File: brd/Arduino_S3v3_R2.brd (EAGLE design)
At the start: 49.1 x 49.1 mm, 35 parts, among them J4 USB_B_PTH, U1 FT232RL, U2 ATMEGA328P_TQFP, U3 ADXL337, Y2 CSTNE16M0V51Z000R0

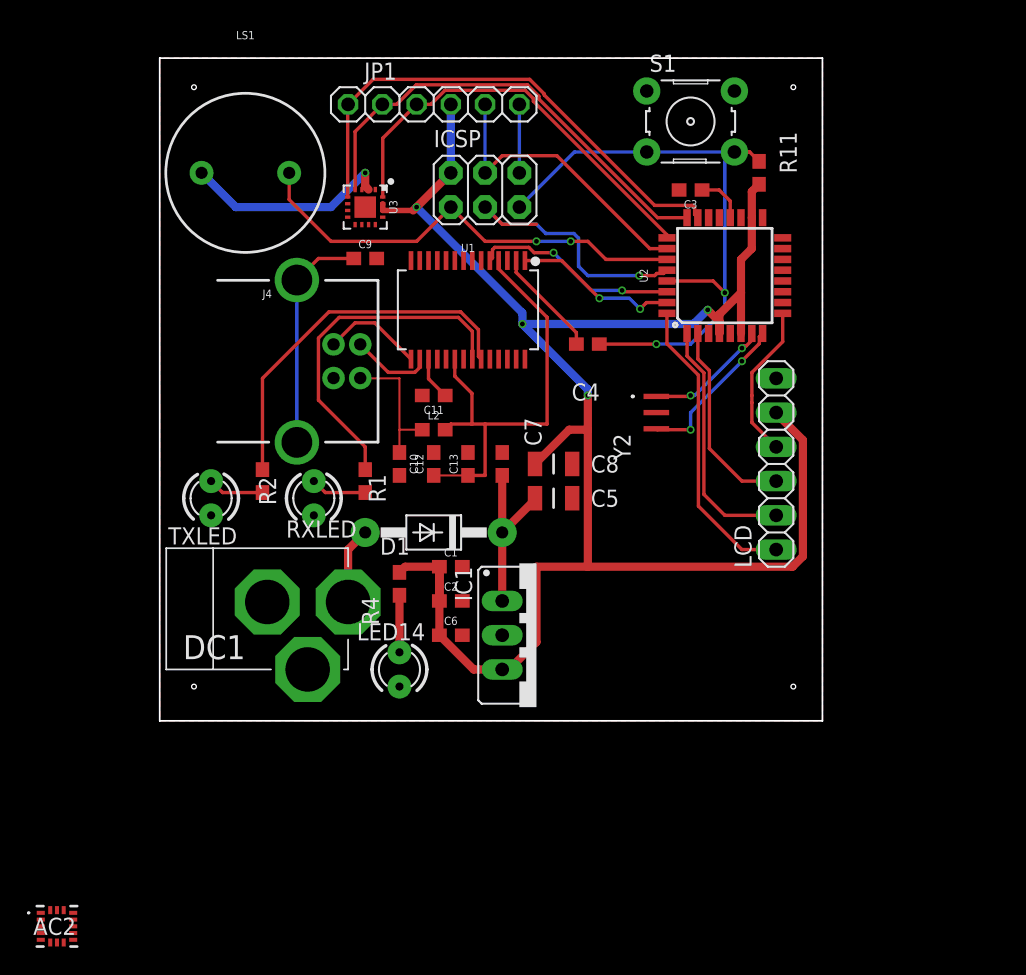
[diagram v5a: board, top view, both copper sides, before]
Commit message: new accel, 3.3v regulator, final draft
Ready for Board Review.
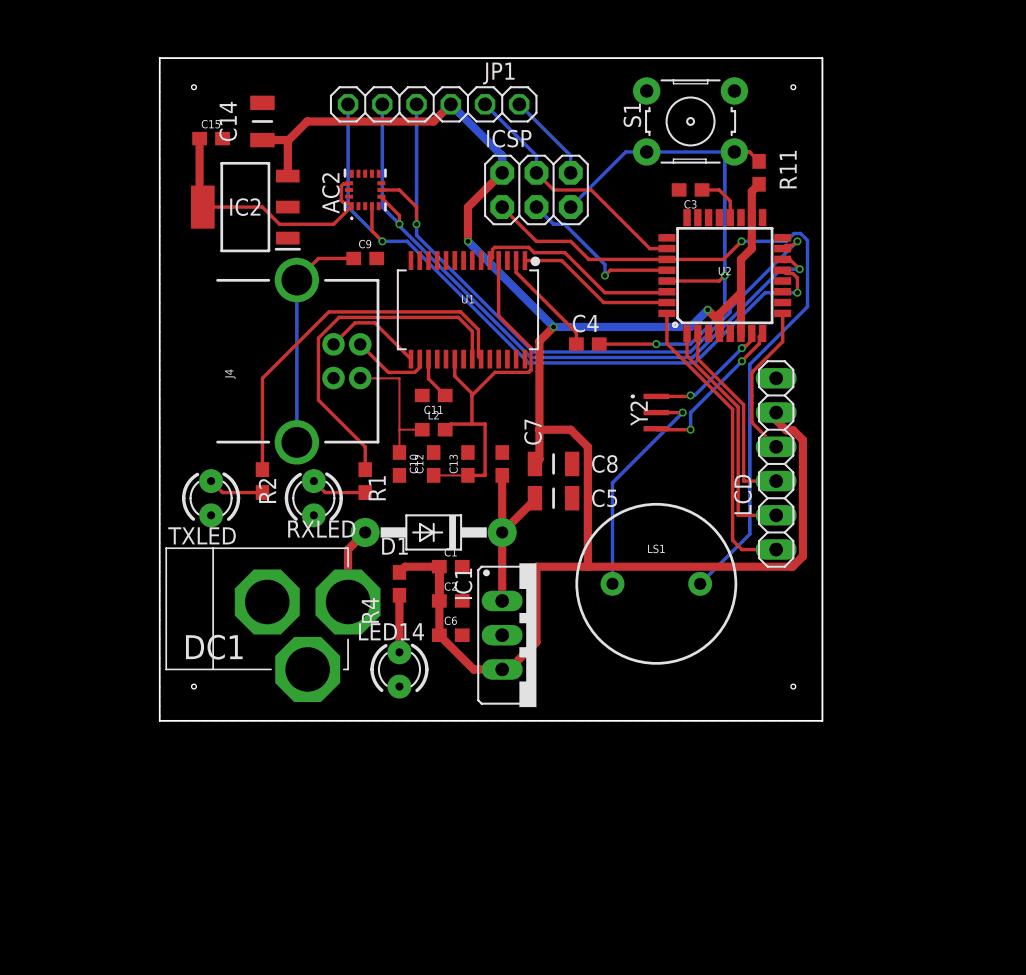
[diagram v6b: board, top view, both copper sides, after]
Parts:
- removed U3: ADXL337, SparkFun-Sensors:LFCSP-16-3X3
- added C14: GRM31CR61A107ME05L, SamacSys_Parts:CAPC3216X180N
- added C15: 10uF, SparkFun-Capacitors:0603
- added IC2: LM1117IMP-3.3_NOPB, SamacSys_Parts:SOT230P700X180-4N
- moved AC2 59.2 mm to (15.2, 39.4), turned to 90 degrees
- moved LS1 43.1 mm to (36.8, 10.2)
- moved ICSP 3.81 mm to (27.9, 39.4)
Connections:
- net N$5 renamed VBUS
- removed net GND_1: AC2.5
- removed net GND_2: AC2.12
- removed net VDD: AC2.14
- removed net VDDIO: AC2.1
- removed net XOUT: JP1.3, U2.25, U3.16
- removed net YOUT: JP1.2, U2.24, U3.4
- removed net ZOUT: JP1.1, U2.23, U3.5
- new net 3.3V: AC2.1, AC2.14, C15.1, IC2.4
- new net ACC_SCL: AC2.4, JP1.1, U2.13
- new net ACC_SDA: AC2.6, JP1.2, U2.14
- new net ACC_SDO: AC2.7, JP1.3, U2.15
- net +5V: now also C14.1, IC2.3; no longer U3.14, U3.15
- net GND: now also AC2.10, AC2.12, AC2.5, AC2.8, C14.2, C15.2, IC2.1; no longer U3.2, U3.6, U3.7
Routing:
- net ACC_SCL: track 0.00 -> 53.2 mm, vias 0 -> 2
- net ACC_SDO: track 0.00 -> 50.8 mm, vias 0 -> 2
- net ACC_SDA: track 0.00 -> 50.1 mm, vias 0 -> 2
- net ZOUT: track 38.2 -> 0.00 mm
- net YOUT: track 34.6 -> 0.00 mm
- net XOUT: track 31.7 -> 0.00 mm
- net BUZZ: track 33.9 -> 54.0 mm, vias 2 -> 1
- net 3.3V: track 0.00 -> 20.0 mm
- net +5V: track 137.2 -> 149.9 mm, vias 4 -> 3
- net N$15: track 21.3 -> 12.4 mm
- net RESET: track 47.1 -> 42.8 mm
- net VBUS: track 34.3 -> 30.4 mm
- net POTIN: track 21.9 -> 18.7 mm
- net GND: track 21.2 -> 23.5 mm
- net LCD_SDO: track 18.5 -> 17.9 mm
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- added copper zone on layer 16, net GND
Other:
- board text added: "Devon Mickels Hannah Mortimer"
- board text added: "ECE-411-Dice"
- board text added: "Jack Chen Nicole Fellows"
- board text removed: "Devon Mickels Hannah Mortimer Nicole Fellows Jack Chen"

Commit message: Modified according to Desgin Review w/ Greenberg
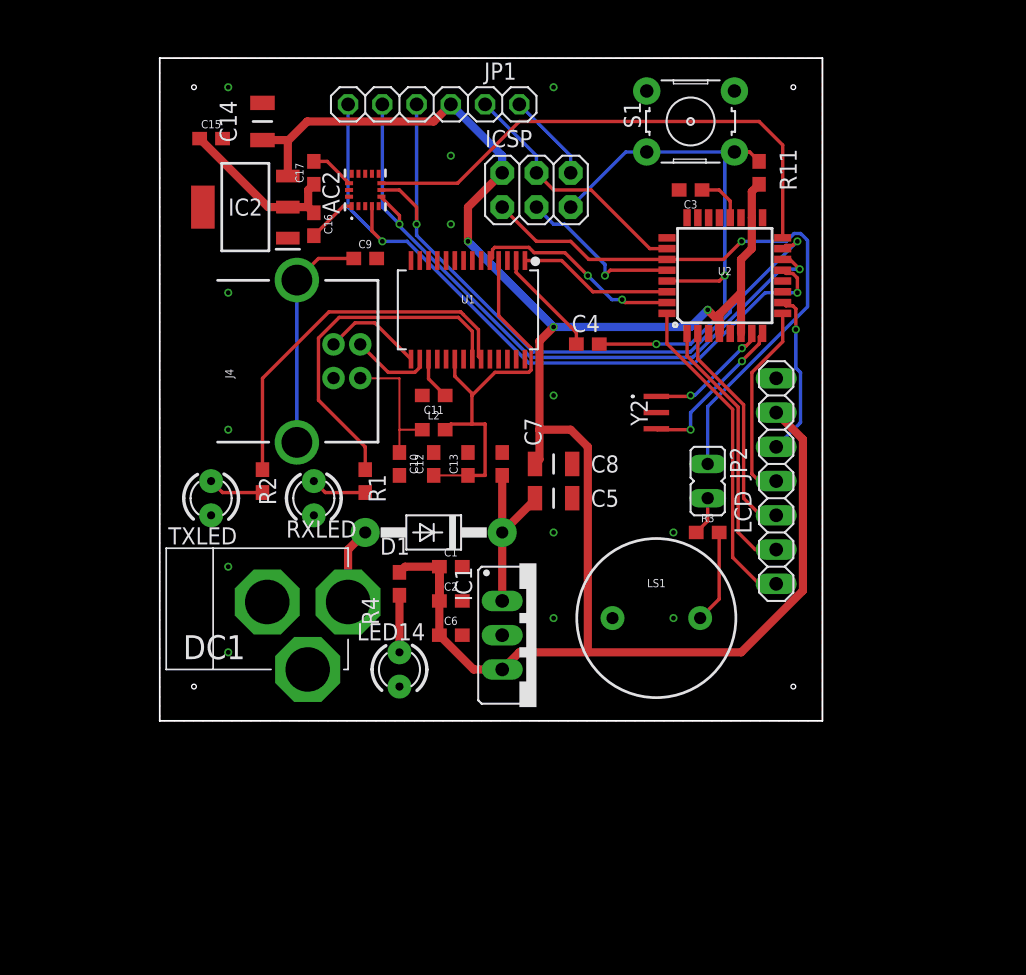
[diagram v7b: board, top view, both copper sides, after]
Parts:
- added C16, C17: 0.1uF, SparkFun-Capacitors:0603
- added JP2: JUMPER, jumper:JP1
- added R3: 100, SparkFun-Resistors:0603
- IC1: value (none) -> L7805CV
- JP1: value (none) -> DEBUG PINOUT
- LCD: value (none) -> LCD PINOUT; device pinhead:1X06 -> pinhead:1X07
- S1: value (none) -> RESET SWITCH
- moved LS1 2.54 mm to (36.8, 7.62)
- moved LCD 1.27 mm to (45.7, 17.8)
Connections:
- new net ACC_CS: AC2.8, U2.16
- new net ACC_INT1: AC2.11
- new net ACC_INT2: AC2.9
- new net N$11: LCD.5, U2.10
- new net N$12: JP2.2, R3.1
- new net N$14: LS1.+, R3.2
- new net N$5: AC2.14, C17.2
- new net N$7: AC2.1, C16.2
- net +5V: now also LCD.6; no longer LCD.5
- net 3.3V: now also C16.1, C17.1, IC2.2; no longer AC2.1, AC2.14, IC2.4
- net BUZZ: now also JP2.1; no longer LS1.+
- net GND: now also LCD.7; no longer AC2.8, LCD.6
- net RXD: now also U2.31; no longer U2.30
- net TXD: now also U2.30; no longer U2.31
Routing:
- net ACC_CS: track 0.00 -> 39.3 mm
- net GND: track 23.5 -> 6.66 mm, vias 1 -> 13
- net N$11: track 0.00 -> 12.3 mm, vias 0 -> 1
- net BUZZ: track 54.0 -> 44.9 mm
- net 3.3V: track 20.0 -> 12.6 mm
- net N$14: track 0.00 -> 6.93 mm
- net +5V: track 149.9 -> 154.2 mm
- net N$7: track 0.00 -> 3.72 mm
- net LCD_SCL: track 11.6 -> 14.9 mm
- net N$5: track 0.00 -> 3.28 mm
- net N$12: track 0.00 -> 2.89 mm
- net LCD_SDO: track 17.9 -> 19.7 mm
- net LCD_SDA: track 14.8 -> 16.6 mm
- net LCD_CS: track 22.4 -> 24.2 mm
- net RXD: track 15.3 -> 15.6 mm, vias 0 -> 2
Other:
- board text added: "ece-411-t3-All_In_One_Dice"
- board text removed: "ECE-411-Dice"

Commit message: Modified after meeting w/ Team 13
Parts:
- JP1: device adafruit:1X06 -> pinhead:1X07
- moved C1 40.2 mm to (44.5, 44.5)
- moved C2 40.2 mm to (44.5, 41.9)
- moved C6 40.2 mm to (44.5, 39.4)
- moved C8 15.3 mm to (30.5, 3.81), turned to 270 degrees
- moved C5 10.9 mm to (20.3, 10.2), turned to 180 degrees
- moved C9 10.2 mm to (5.08, 34.3), turned to 180 degrees
- moved R4 7.41 mm to (21.6, 3.81), turned to 270 degrees
- moved R11 4.58 mm to (41.9, 44.5)
- moved R3 4.58 mm to (36.8, 16.5), turned to 180 degrees
- moved C4 4.58 mm to (29.2, 31.8), turned to 90 degrees
- moved Y2 3.81 mm to (33.0, 22.9)
- moved C15 3.59 mm to (6.35, 45.7)
- moved C3 2.84 mm to (41.9, 40.6), turned to 90 degrees
- moved S1 2.84 mm to (36.8, 43.2), turned to 90 degrees
- moved C14 2.84 mm to (10.2, 45.7), turned to 180 degrees
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- renumbered LED14 to PWR
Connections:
- net +5V: now also JP1.5; no longer JP1.4
- net ACC_CS: now also JP1.4
- net GND: now also JP1.7; no longer JP1.6
- net POTIN: now also JP1.6; no longer JP1.5
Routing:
- net +5V: track 154.2 -> 142.4 mm
- net GND: track 6.66 -> 0.00 mm, vias 13 -> 18
- net RESET: track 42.8 -> 49.2 mm
- net N$14: track 6.93 -> 11.1 mm
- net N$4: track 8.05 -> 3.93 mm
- net N$1: track 9.31 -> 13.1 mm
- net N$6: track 11.9 -> 15.0 mm
- net POTIN: track 18.7 -> 17.1 mm
- net 3.3V: track 12.6 -> 11.5 mm
- net N$16: track 3.67 -> 2.56 mm
- net N$5: track 3.28 -> 4.22 mm
- net N$9: track 7.52 -> 8.26 mm
- net VIN: track 12.9 -> 13.5 mm
- net ACC_CS: track 39.3 -> 38.6 mm, vias 0 -> 3
- net N$7: track 3.72 -> 3.19 mm
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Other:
- board text added: "Devon Mickels Jack Chen Nicole Fellows Hannah Mortimer"
- board text removed: "Devon Mickels Hannah Mortimer"
- board text removed: "Jack Chen Nicole Fellows"
